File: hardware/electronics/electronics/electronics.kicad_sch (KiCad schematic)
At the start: 7 parts, among them J1 Conn_Coaxial_Small, U1 RFM95W-915S2, U2 BME280, U3 ICM-20602, U4 SD Card mini module, U5 ESP32-C3 SUPERMINI, U6 GPS M8N

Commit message: doc: update general documentations
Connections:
- net CLK_SD is gone; now on net SCK: U4.4 (CLK), U5.4 (GPIO4)
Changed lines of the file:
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@@
-		)
-	)
-	(label "CLK_SD"
-		(at 129.54 86.36 180)
-		(effects
-			(font
-				(size 1.27 1.27)
-			)
-			(justify right bottom)
 		)
 	)
@@
 		)
 	)
+	(label "SCK"
+		(at 203.2 48.26 180)
+		(effects
+			(font
+				(size 1.27 1.27)
+			)
+			(justify right bottom)
+		)
+	)
 	(label "CS_SD"
 		(at 203.2 53.34 180)
@@
 		)
 	)
-	(label "CLK_SD"
-		(at 203.2 48.26 180)
-		(effects
-			(font
+	(label "SCK"
+		(at 129.54 86.36 180)
+		(effects
+			(font

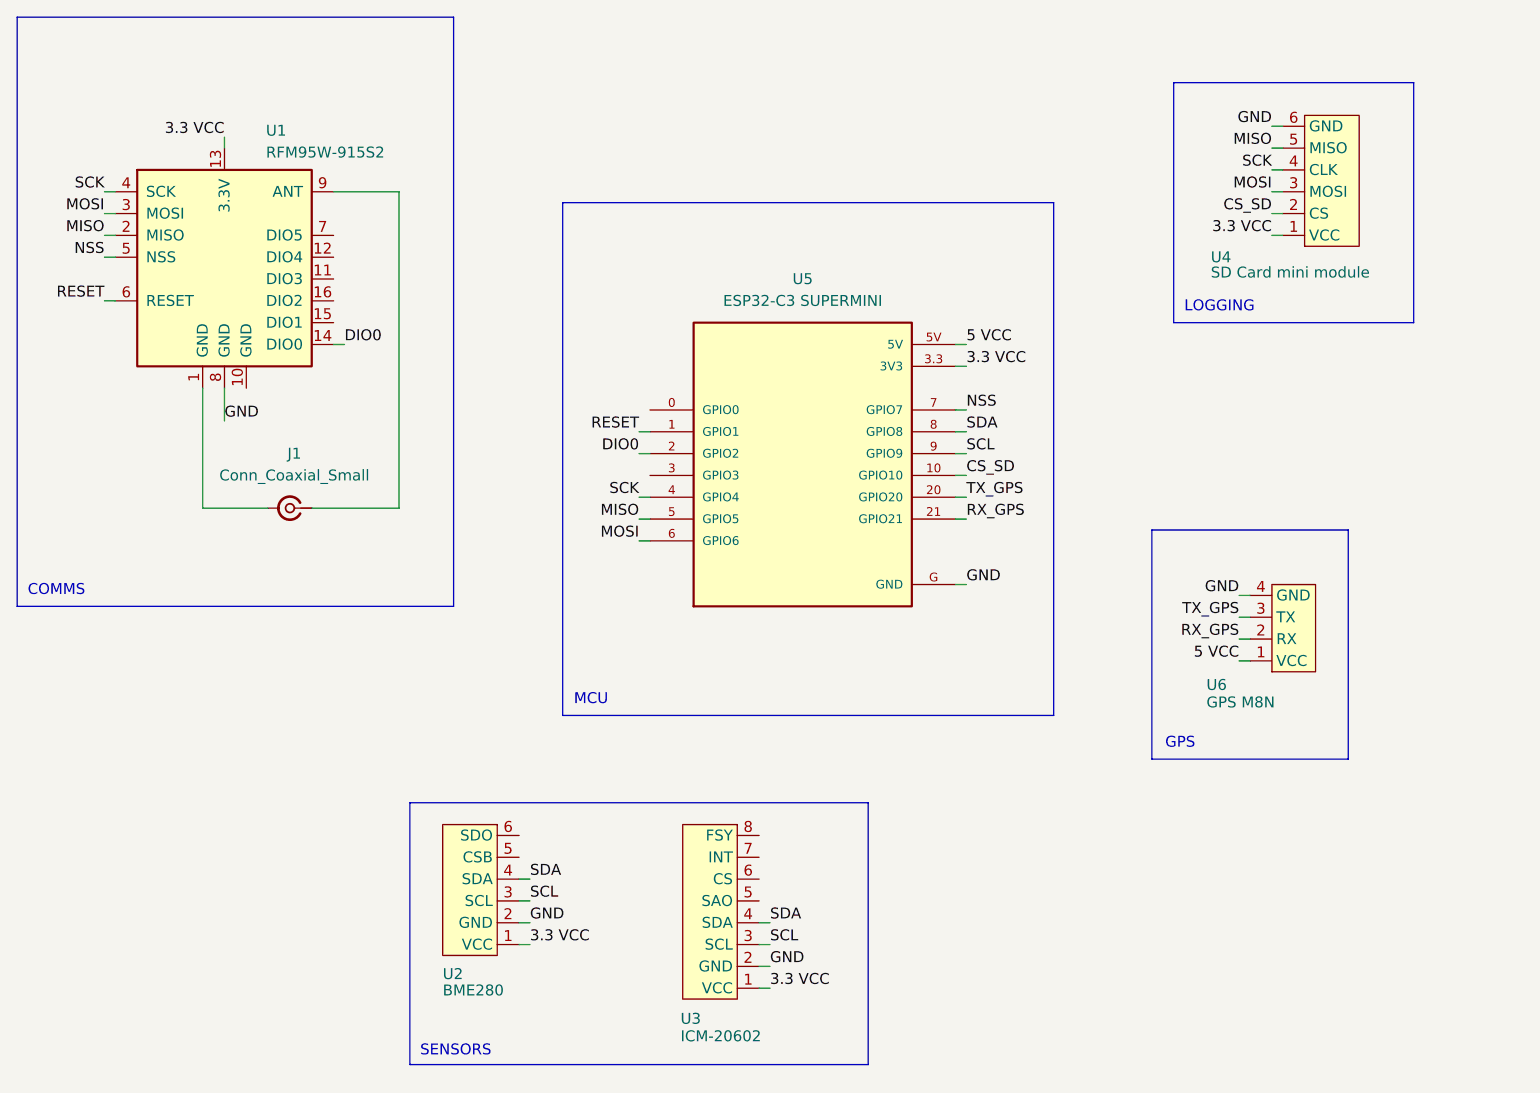
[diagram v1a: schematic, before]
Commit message: docs: update buzzer type to active (digitalWrite, no PWM)
- hardware.md: active buzzer, GPIO (digitalWrite), LEDC bug note updated
- firmware.md: LEDC bug workaround corrected for active buzzer
- software.md: BuzzerModule description updated
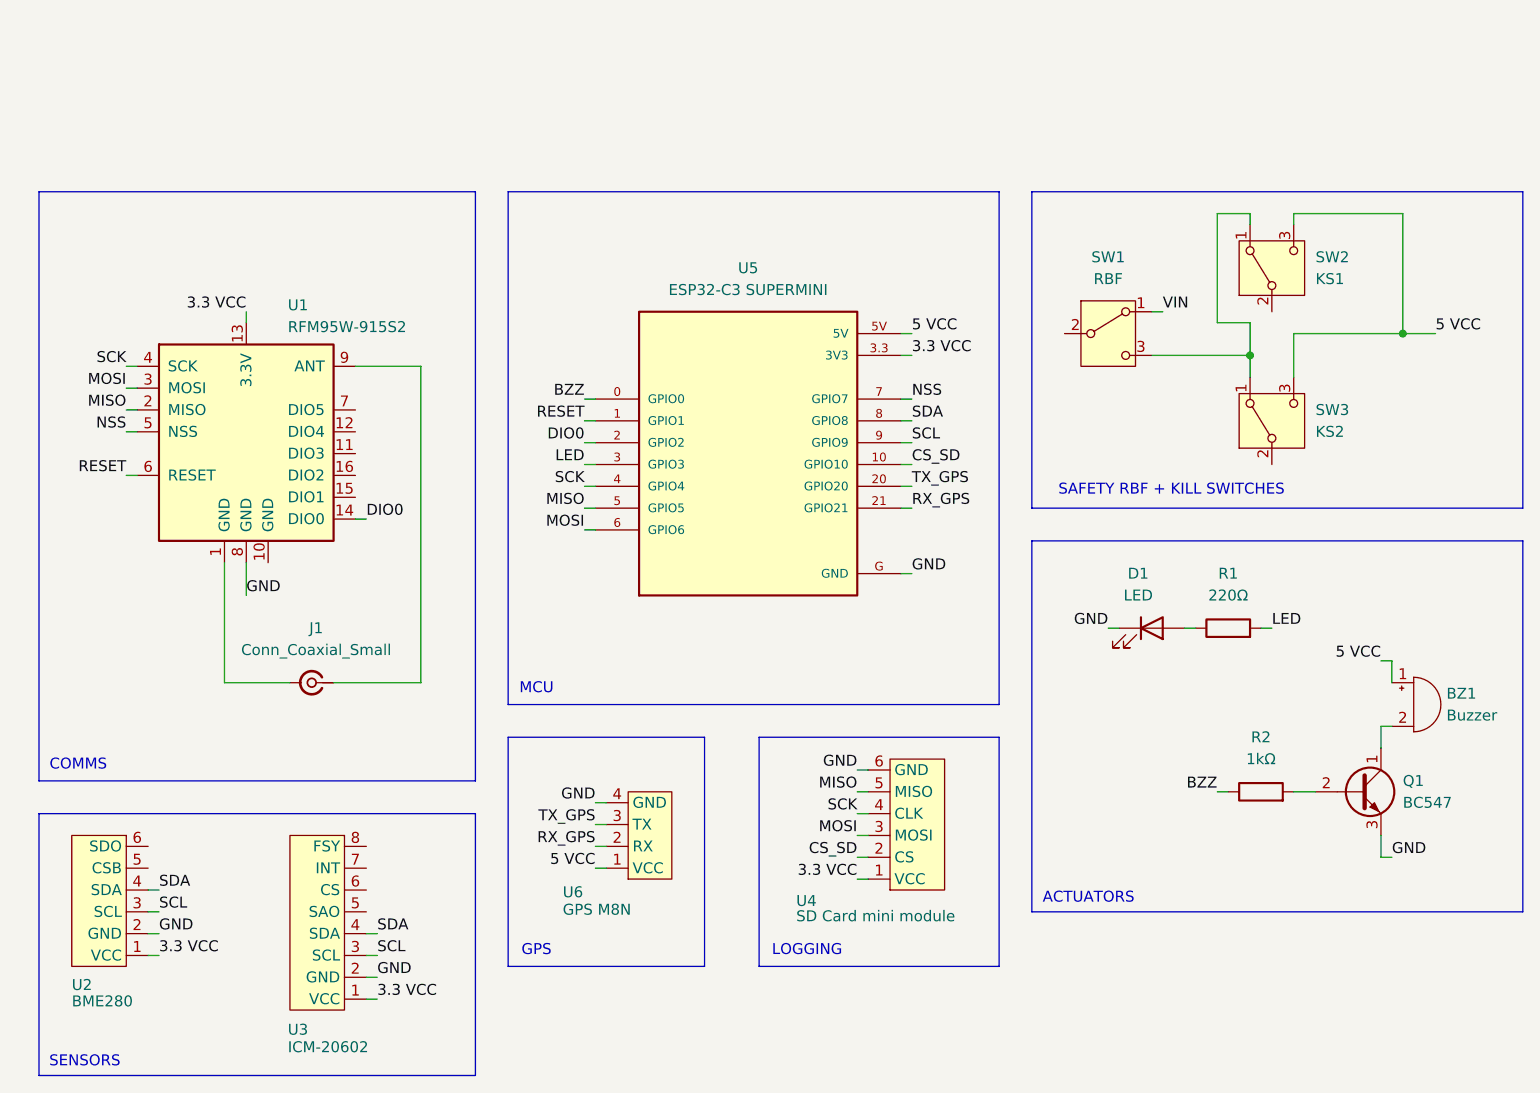
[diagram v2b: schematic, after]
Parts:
- added BZ1: Buzzer, symbol Device:Buzzer
- added D1: LED, LED_THT:LED_D3.0mm, symbol Device:LED
- added Q1: BC547, Package_TO_SOT_THT:TO-92_Inline, symbol Transistor_BJT:BC547
- added R1: 220Ω, Resistor_THT:R_Axial_DIN0204_L3.6mm_D1.6mm_P5.08mm_Horizontal, symbol Device:R
- added R2: 1kΩ, Resistor_THT:R_Axial_DIN0204_L3.6mm_D1.6mm_P5.08mm_Horizontal, symbol Device:R
- added SW1: RBF, Button_Switch_THT:SW_XKB_DM1-16UC-1, symbol Switch:SW_SPDT
- added SW2: KS1, Button_Switch_THT:SW_XKB_DM1-16UC-1, symbol Switch:SW_SPDT
- added SW3: KS2, Button_Switch_THT:SW_XKB_DM1-16UC-1, symbol Switch:SW_SPDT
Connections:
- net 5 VCC: now also BZ1.1 (+), SW2.3 (C), SW3.3 (C)
- net GND: now also D1.1 (K), Q1.3 (E)
- net BZZ: now reaches U5.0 (GPIO0)
- net BZZ: now also R2.1
- net LED: now reaches U5.3 (GPIO3)
- net LED: now also R1.2
- new net: BZ1.2 (-), Q1.1 (C)
- new net: SW1.3 (C), SW2.1 (A), SW3.1 (A)
- new net: Q1.2 (B), R2.2
- new net: D1.2 (A), R1.1
- new net VIN: SW1.1 (A)
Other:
- note added: "ACTUATORS"
- note added: "SAFETY RBF + KILL SWITCHES"
- moved on the sheet: J1, U1, U2, U3, U4, U5, U6
